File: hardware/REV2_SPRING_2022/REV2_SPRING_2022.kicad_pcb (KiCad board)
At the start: 2 copper layers, 108 x 304.8 mm, 52 parts, among them J101 Screw_Terminal_01x02, J102 Screw_Terminal_01x02, J103 Conn_01x02_Female, J104 Screw_Terminal_01x02, J105 Conn_01x02_Female, J107 Screw_Terminal_01x02, J109 Conn_01x02_Female, J110 Conn_01x02_Female, Q101 Q_NMOS_GDS, Q102 Q_NMOS_GDS, U1 Teensy3.6_All_Pins, U2 PA16165_Breakout, U201 TPS2113ADRBR, U3 MPL3115A2_Breakout, U301 TPS2113ADRBR, U4 BNO055_Breakout, U5 RFM69HCW_Breakout

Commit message: wip
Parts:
- moved D105 62.8 mm to (129.0, 74.9), turned to 270 degrees
- moved D106 58.9 mm to (159.5, 74.8), turned to 270 degrees
- moved D104 54.8 mm to (135.1, 74.9), turned to 270 degrees
- moved D101 54.1 mm to (153.4, 74.9), turned to 270 degrees
- moved D103 51.8 mm to (141.2, 74.9), turned to 270 degrees
- moved D102 51.5 mm to (147.3, 74.9), turned to 270 degrees
- moved R108 50.2 mm to (129.0, 67.3), turned to 90 degrees
- moved R113 46.5 mm to (159.5, 67.2), turned to 90 degrees
- moved R107 40.9 mm to (135.1, 67.3), turned to 90 degrees
- moved R104 40.0 mm to (153.4, 67.3), turned to 90 degrees
- moved R106 36.7 mm to (141.2, 67.3), turned to 90 degrees
- moved R105 36.4 mm to (147.3, 67.3), turned to 90 degrees
- moved U2 6.83 mm to (139.0, 144.2)
- moved U5 3.89 mm to (137.0, 105.8)
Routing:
- net /SCL2: track 46.2 -> 0.00 mm, vias 3 -> 0
- net /PWM: track 32.3 -> 0.00 mm
- net /SCK: track 65.6 -> 60.9 mm, vias 2 -> 0
- net /CS0: track 14.5 -> 10.6 mm
- net /MOSI0: track 14.5 -> 10.6 mm
- net /MISO0: track 14.5 -> 10.6 mm
- net /3.3V: track 218.6 -> 214.7 mm

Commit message: wip starting to look good
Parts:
- moved J105 93.9 mm to (79.0, 66.2)
- moved J107 93.9 mm to (74.0, 25.2)
- moved D106 93.3 mm to (252.8, 75.0)
- moved R113 93.3 mm to (252.8, 67.5)
- moved J103 92.3 mm to (99.0, 66.2)
- moved J104 92.3 mm to (99.0, 25.8)
- moved R112 91.2 mm to (136.5, 71.5)
- moved R111 89.8 mm to (156.0, 70.0)
- moved D101 88.3 mm to (241.7, 75.1)
- moved R104 88.3 mm to (241.7, 67.5)
- moved J109 86.6 mm to (149.0, 66.2)
- moved J102 86.4 mm to (128.8, 24.8)
- moved J110 86.4 mm to (129.0, 66.2)
- moved J101 85.9 mm to (149.0, 24.7)
- moved Q102 85.6 mm to (128.5, 76.8)
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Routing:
- net /V_EMATCH_TO_KEY_SWITCH: track 298.5 -> 187.7 mm
- net /LED_0: track 0.00 -> 59.5 mm
- net /LED_3: track 0.26 -> 45.8 mm
- net /LED_4: track 0.01 -> 44.9 mm
- net /LED_1: track 0.14 -> 40.6 mm
- net /SCL2: track 0.00 -> 38.6 mm, vias 0 -> 1
- net /V_EMATCH: track 168.3 -> 131.5 mm
- net /PWM: track 0.00 -> 28.4 mm, vias 0 -> 1
- net /LED_2: track 0.12 -> 28.5 mm
- net /3.3V: track 214.7 -> 231.3 mm, vias 5 -> 7
- net /EMATCH_2+: track 57.3 -> 44.1 mm
- net /EMATCH_1+: track 56.6 -> 44.3 mm
- net /TX1: track 10.3 -> 0.64 mm
- net /RX1: track 10.3 -> 0.64 mm
- net /SCK: track 60.9 -> 66.7 mm, vias 0 -> 2
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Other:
- board text removed: "Ian Eykamp Marc Eftimie Charlie Babe Nov. 24, 2021 Pheonix IV Rev. 1"

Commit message: wip
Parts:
- moved D105 95.5 mm to (102.1, 82.3), turned to 180 degrees
- moved R108 90.7 mm to (107.8, 82.2), turned to 0 degrees
- moved R110 11.5 mm to (96.2, 82.5), turned to 90 degrees
- moved U2 0.50 mm to (139.0, 143.8)
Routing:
- net GND: track 151.8 -> 22.4 mm, vias 5 -> 1
- net /KEY_SWITCH_DIGITAL: track 43.2 -> 85.1 mm, vias 0 -> 1
- net /3.3V: track 231.3 -> 244.4 mm
- net /V_EMATCH_TO_KEY_SWITCH: track 187.7 -> 198.6 mm
- net /TX1: track 0.64 -> 7.53 mm
- net /RX1: track 0.64 -> 7.53 mm
- net Net-(D105-Pad1): track 5.59 -> 0.00 mm

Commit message: wip switch wire terminals
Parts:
- moved J107 5.09 mm to (79.0, 24.3), turned to 180 degrees
- moved J104 1.45 mm to (99.0, 24.3)
- moved J101 0.50 mm to (149.0, 24.2)
- moved J102 0.50 mm to (128.8, 24.2)
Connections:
- J101 pad 1: /V_EMATCH -> /EMATCH_1+
- J101 pad 2: /EMATCH_1+ -> /V_EMATCH
- J102 pad 1: /V_EMATCH -> /EMATCH_2+
- J102 pad 2: /EMATCH_2+ -> /V_EMATCH
- J107 pad 1: /V_EMATCH -> /V_EMATCH_TO_KEY_SWITCH
- J107 pad 2: /V_EMATCH_TO_KEY_SWITCH -> /V_EMATCH
- J109 pad 1: /V_EMATCH -> /EMATCH_1+
- J109 pad 2: /EMATCH_1+ -> /V_EMATCH
- J110 pad 1: /V_EMATCH -> /EMATCH_2+
- J110 pad 2: /EMATCH_2+ -> /V_EMATCH
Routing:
- net /V_EMATCH: track 131.5 -> 133.6 mm
- net /KEY_SWITCH_DIGITAL: track 85.1 -> 86.6 mm
- net /3.3V: track 244.4 -> 245.9 mm
- net /V_EMATCH_TO_KEY_SWITCH: track 198.6 -> 199.6 mm

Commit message: wip
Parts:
- moved R112 15.0 mm to (121.5, 71.5), turned to 0 degrees
- moved R111 14.6 mm to (141.5, 71.5), turned to 0 degrees
- moved R110 5.50 mm to (96.2, 88.0)
- moved J101 3.00 mm to (146.0, 24.2)
- moved J102 3.00 mm to (125.8, 24.2)
- moved J109 3.00 mm to (146.0, 66.2)
- moved J110 3.00 mm to (126.0, 66.2)
- moved R103 1.41 mm to (147.5, 82.8), turned to 180 degrees
- moved R109 1.41 mm to (127.5, 82.8), turned to 180 degrees
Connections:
- J105 pad 1: /V_EMATCH_TO_KEY_SWITCH -> /V_EMATCH
- J105 pad 2: /V_EMATCH -> /V_EMATCH_TO_KEY_SWITCH
- J107 pad 1: /V_EMATCH_TO_KEY_SWITCH -> /V_EMATCH
- J107 pad 2: /V_EMATCH -> /V_EMATCH_TO_KEY_SWITCH
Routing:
- net /V_EMATCH: track 133.6 -> 239.1 mm
- net /E-MATCH_TRIGGER_1: track 0.00 -> 68.1 mm, vias 0 -> 1
- net /E-MATCH_TRIGGER_2: track 0.00 -> 53.2 mm, vias 0 -> 1
- net /EMATCH_2+: track 44.6 -> 58.6 mm
- net /EMATCH_1+: track 44.5 -> 58.5 mm
- net /LED_4: track 44.9 -> 36.9 mm
- net /LED_2: track 28.5 -> 22.5 mm
- net /LED_0: track 59.5 -> 55.3 mm
- net /LED_1: track 40.6 -> 36.7 mm
- net Net-(D105-Pad1): track 0.00 -> 3.67 mm
- net /LED_3: track 45.8 -> 42.2 mm
- net /V_EMATCH_TO_KEY_SWITCH: track 199.6 -> 198.0 mm
- net /KEY_SWITCH_DIGITAL: track 86.6 -> 88.1 mm
- net /3.3V: vias 7 -> 5

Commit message: wip layout almost finished
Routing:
- net /TPS_1_STAT: track 3.80 -> 103.6 mm, vias 0 -> 2
- net /TPS_2_STAT: track 5.71 -> 90.2 mm, vias 0 -> 2
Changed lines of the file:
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@@
     (thickness 1.6)
     (drawings 28)
-    (tracks 267)
+    (tracks 291)
     (zones 0)
     (modules 52)
@@
   (segment (start 140.189 168.974) (end 140.062 168.847) (width 0.4318) (layer F.Cu) (net 35) (status 30))
   (segment (start 143.618 168.974) (end 140.189 168.974) (width 0.4318) (layer F.Cu) (net 35) (status 30))
-  (via (at 121 167.25) (size 0.8) (drill 0.4) (layers F.Cu B.Cu) (net 35))
-  (segment (start 120.927 167.323) (end 121 167.25) (width 0.4318) (layer F.Cu) (net 35))
-  (segment (start 116.7075 167.323) (end 120.927 167.323) (width 0.4318) (layer F.Cu) (net 35) (status 10))
-  (segment (start 121 167.25) (end 124.75 167.25) (width 0.4318) (layer B.Cu) (net 35))
-  (segment (start 124.75 167.25) (end 126.75 165.25) (width 0.4318) (layer B.Cu) (net 35))
   (via (at 132.5 164.5) (size 0.8) (drill 0.4) (layers F.Cu B.Cu) (net 35))
-  (segment (start 127.5 164.5) (end 132.5 164.5) (width 0.4318) (layer B.Cu) (net 35))
-  (segment (start 126.75 165.25) (end 127.5 164.5) (width 0.4318) (layer B.Cu) (net 35))
   (segment (start 135.4265 167.4265) (end 136.765 167.4265) (width 0.4318) (layer F.Cu) (net 35) (status 20))
   (segment (start 132.5 164.5) (end 135.4265 167.4265) (width 0.4318) (layer F.Cu) (net 35))
@@
   (segment (start 148.54 82.71) (end 148.5 82.75) (width 0.762) (layer F.Cu) (net 15))
   (segment (start 148.54 76.75) (end 148.54 82.71) (width 0.762) (layer F.Cu) (net 15))
+  (segment (start 102.265 98.049) (end 103.5 99.284) (width 0.25) (layer F.Cu) (net 17))
+  (segment (start 103.5 99.284) (end 103.5 132.5) (width 0.25) (layer F.Cu) (net 17))
+  (segment (start 103.5 132.5) (end 107 136) (width 0.25) (layer F.Cu) (net 17))
+  (via (at 110 153.5) (size 0.8) (drill 0.4) (layers F.Cu B.Cu) (net 17))
+  (segment (start 107 150.5) (end 110 153.5) (width 0.25) (layer F.Cu) (net 17))
+  (segment (start 107 136) (end 107 150.5) (width 0.25) (layer F.Cu) (net 17))
+  (segment (start 116.772 172.728) (end 119 170.5) (width 0.25) (layer F.Cu) (net 17))
+  (segment (start 114.845 172.728) (end 116.772 172.728) (width 0.25) (layer F.Cu) (net 17))
+  (segment (start 119 162.5) (end 119 170.5) (width 0.25) (layer B.Cu) (net 17))
+  (segment (start 110 153.5) (end 119 162.5) (width 0.25) (layer B.Cu) (net 17))
+  (via (at 119 170.5) (size 0.8) (drill 0.4) (layers F.Cu B.Cu) (net 17))
+  (via (at 133.5 174) (size 0.8) (drill 0.4) (layers F.Cu B.Cu) (net 19))
+  (segment (start 133.5 174) (end 134.5 174) (width 0.25) (layer F.Cu) (net 19))
+  (segment (start 135.5 173) (end 134.5 174) (width 0.25) (layer F.Cu) (net 19))
+  (segment (start 135.5 172) (end 135.5 173) (width 0.25) (layer F.Cu) (net 19))
+  (via (at 114 153.500006) (size 0.8) (drill 0.4) (layers F.Cu B.Cu) (net 19))
+  (segment (start 125 174) (end 121.5 170.5) (width 0.25) (layer B.Cu) (net 19))
+  (segment (start 102.265 95.509) (end 105.930001 99.174001) (width 0.25) (layer F.Cu) (net 19))
+  (segment (start 112 145) (end 114 147) (width 0.25) (layer F.Cu) (net 19))
+  (segment (start 133.5 174) (end 125 174) (width 0.25) (layer B.Cu) (net 19))
+  (segment (start 105.930001 99.174001) (end 105.930001 117.930001) (width 0.25) (layer F.Cu) (net 19))
+  (segment (start 114 147) (end 114 153.500006) (width 0.25) (layer F.Cu) (net 19))
+  (segment (start 105.930001 117.930001) (end 112 124) (width 0.25) (layer F.Cu) (net 19))
+  (segment (start 112 124) (end 112 145) (width 0.25) (layer F.Cu) (net 19))
+  (segment (start 121.5 170.5) (end 121.5 161.000006) (width 0.25) (layer B.Cu) (net 19))
+  (segment (start 121.5 161.000006) (end 114 153.500006) (width 0.25) (layer B.Cu) (net 19))
   (segment (start 106.73 82.27) (end 106.75 82.25) (width 0.25) (layer F.Cu) (net 28))
   (segment (start 103.087 82.27) (end 106.73 82.27) (width 0.25) (layer F.Cu) (net 28))
@@
   (segment (start 96.25 94.549978) (end 97.800011 96.099989) (width 0.25) (layer F.Cu) (net 34))
   (via (at 97.800011 96.099989) (size 0.8) (drill 0.4) (layers F.Cu B.Cu) (net 34))
+  (via (at 123.499972 167.25) (size 0.8) (drill 0.4) (layers F.Cu B.Cu) (net 35))
+  (segment (start 129.75 167.25) (end 123.499972 167.25) (width 0.4318) (layer B.Cu) (net 35))
+  (segment (start 116.7075 167.323) (end 123.426972 167.323) (width 0.4318) (layer F.Cu) (net 35))
+  (segment (start 123.426972 167.323) (end 123.499972 167.25) (width 0.4318) (layer F.Cu) (net 35))
+  (segment (start 132.5 164.5) (end 129.75 167.25) (width 0.4318) (layer B.Cu) (net 35))
   (segment (start 71 63.65) (end 73.6 66.25) (width 1.524) (layer F.Cu) (net 123))
   (segment (start 71 27.22) (end 71 63.65) (width 1.524) (layer F.Cu) (net 123))

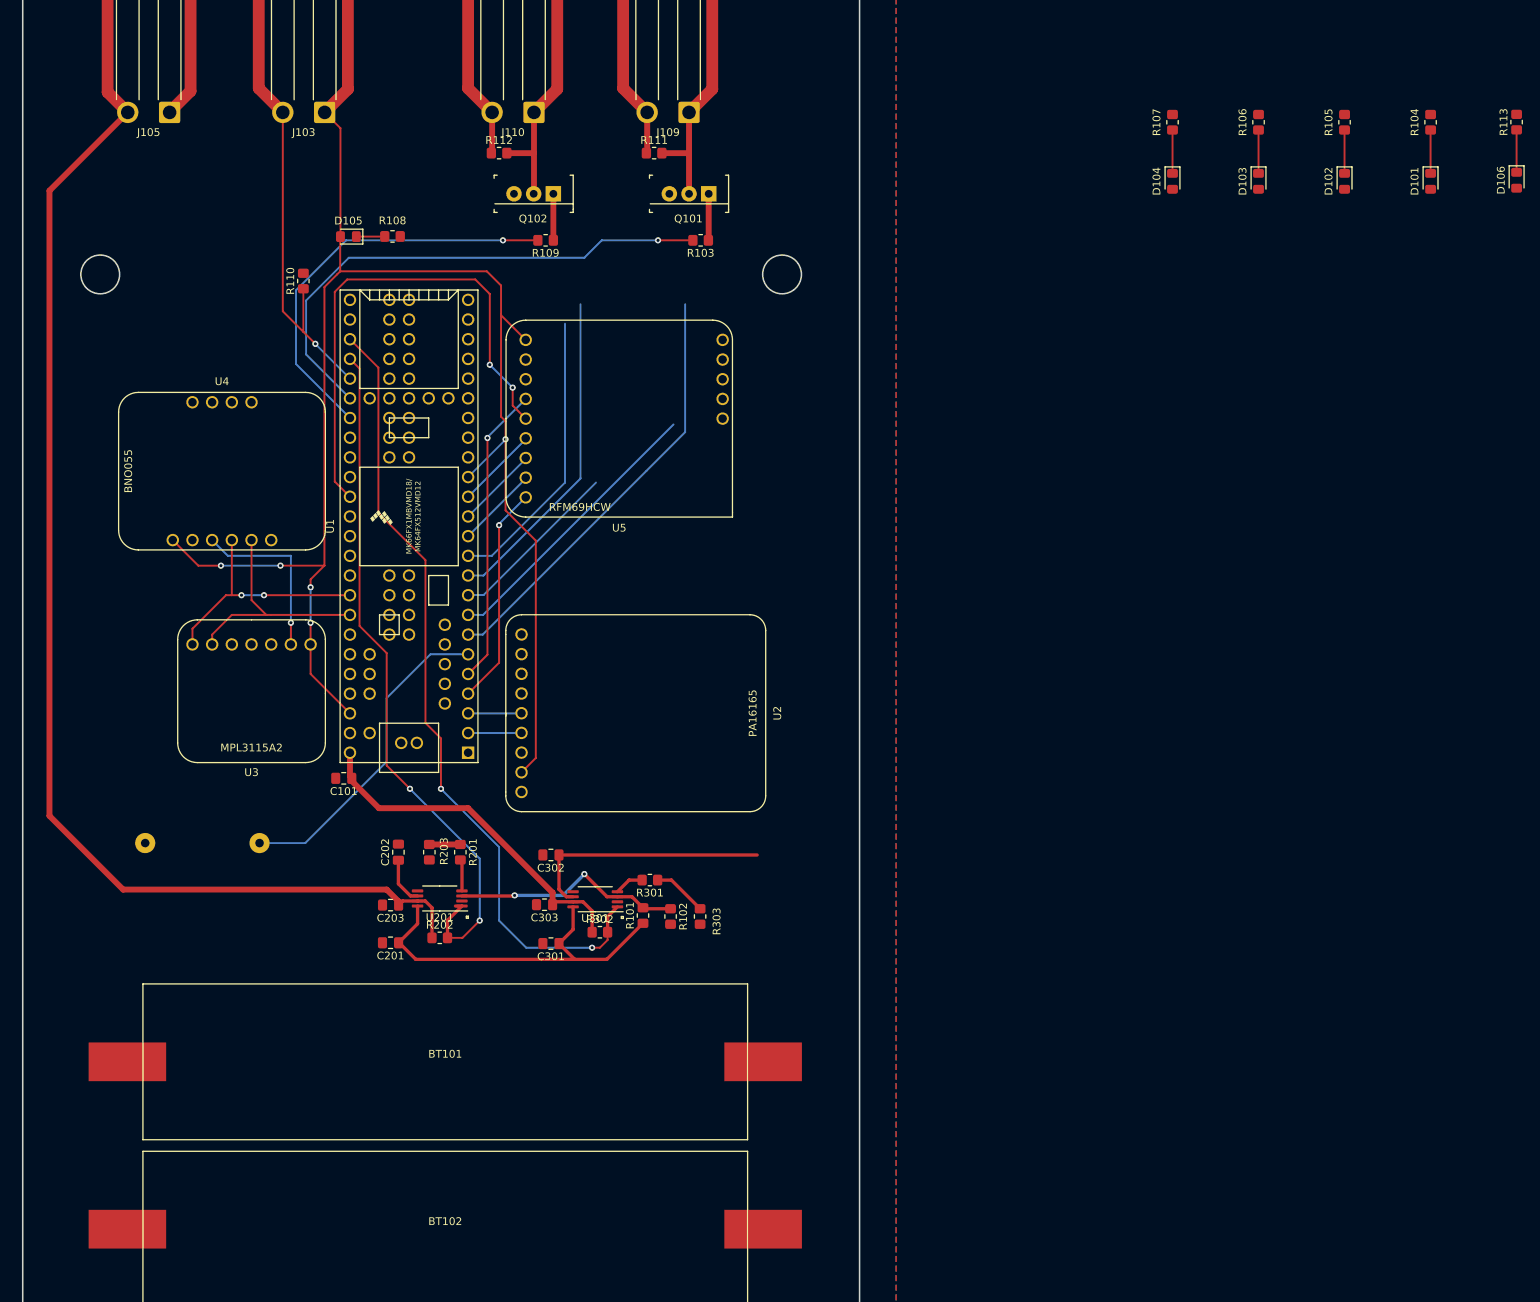
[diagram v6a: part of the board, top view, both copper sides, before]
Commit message: add leds
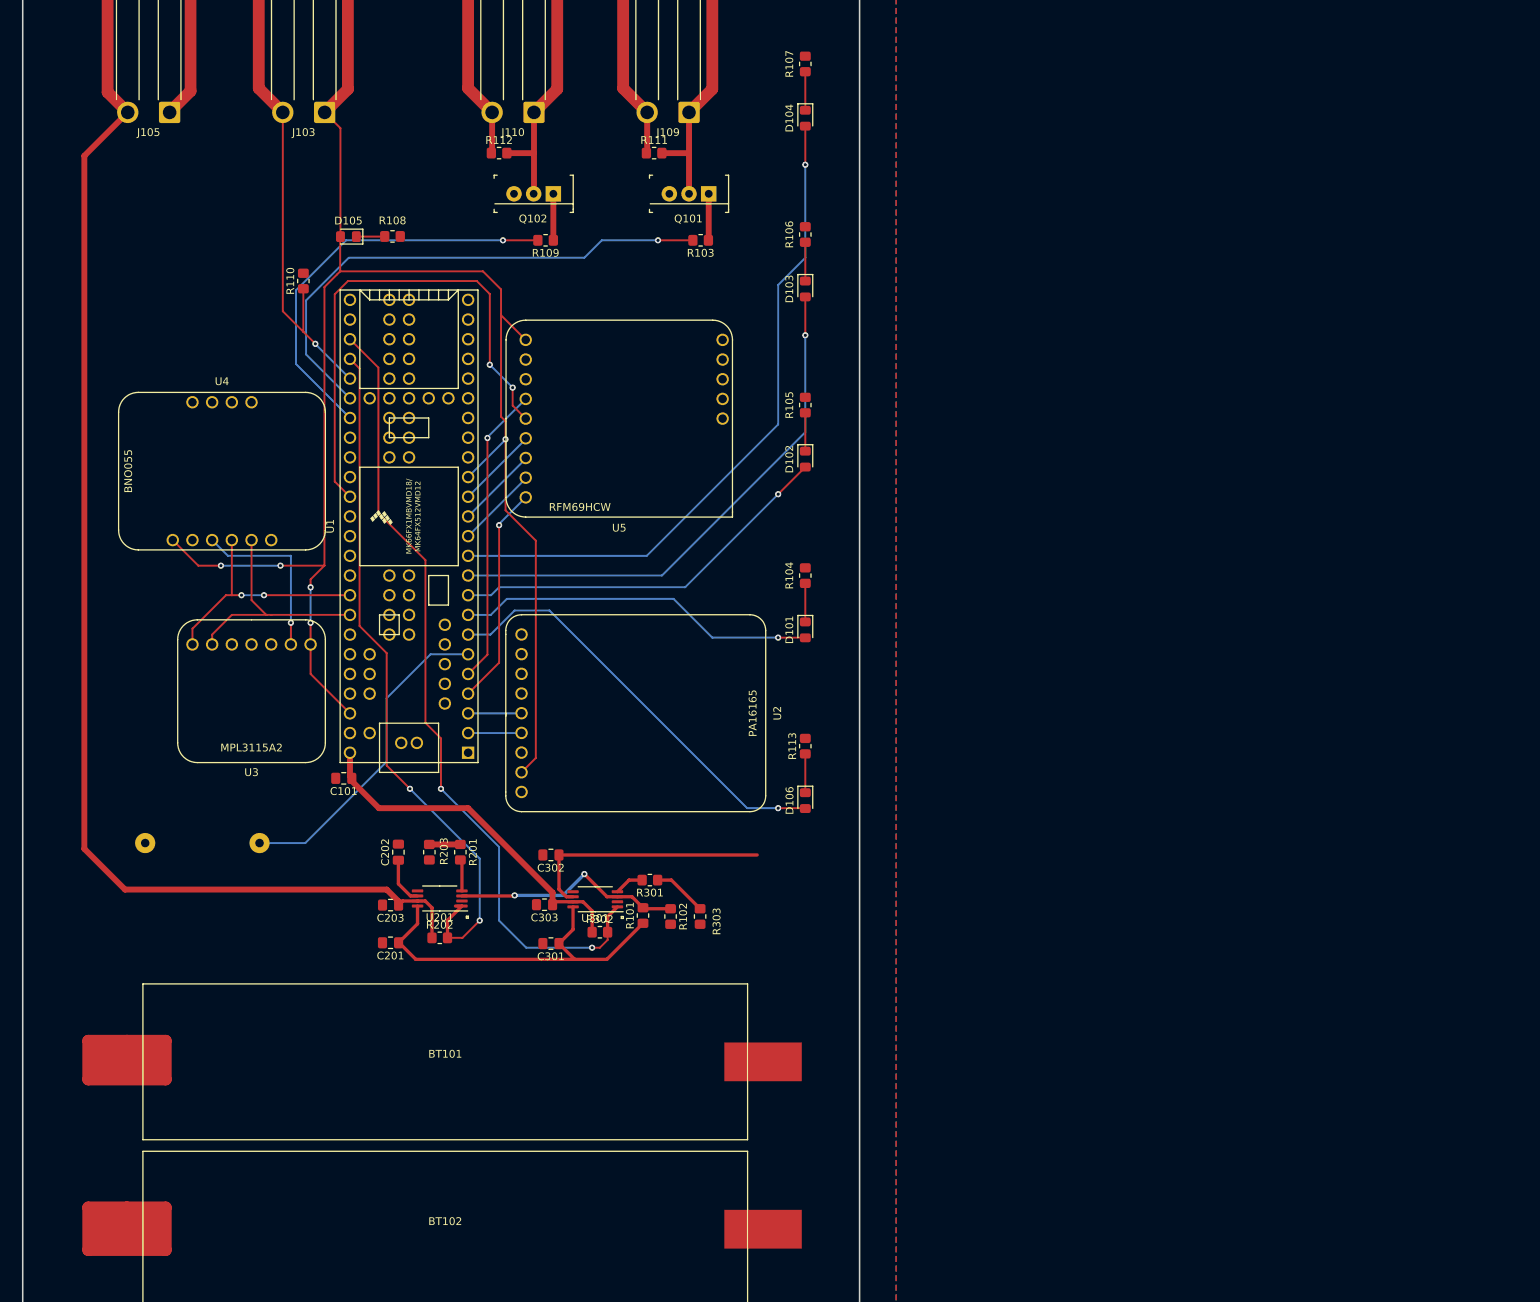
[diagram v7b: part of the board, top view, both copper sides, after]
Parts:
- moved R113 122.1 mm to (161.0, 148.0)
- moved D106 121.7 mm to (161.0, 155.0)
- moved R104 99.6 mm to (161.0, 126.0)
- moved D101 99.3 mm to (161.0, 133.0)
- moved R105 78.5 mm to (161.0, 104.0)
- moved D102 78.2 mm to (161.0, 111.0)
- moved R106 60.2 mm to (161.0, 82.0)
- moved D103 60.1 mm to (161.0, 89.0)
- moved D104 48.1 mm to (161.0, 67.0)
- moved R107 48.0 mm to (161.0, 60.0)
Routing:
- net GND: track 22.4 -> 89.0 mm
- net /LED_4: track 36.9 -> 87.0 mm, vias 0 -> 1
- net /LED_2: track 22.5 -> 50.3 mm, vias 0 -> 1
- net /LED_3: track 42.2 -> 68.6 mm, vias 0 -> 1
- net /LED_1: track 36.7 -> 46.4 mm, vias 0 -> 1
- net /V_EMATCH_TO_KEY_SWITCH: track 198.0 -> 194.1 mm
- net Net-(D102-Pad1): track 5.59 -> 4.95 mm
- net Net-(D104-Pad1): track 5.59 -> 4.97 mm
- net Net-(D101-Pad1): track 5.59 -> 4.97 mm
- net Net-(D103-Pad1): track 5.59 -> 5.00 mm
- net /LED_0: track 55.3 -> 55.4 mm, vias 0 -> 1
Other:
- outline, holes or cut-outs redrawn
